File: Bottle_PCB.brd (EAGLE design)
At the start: 100 x 50 mm, 105 parts, among them Q1 8.000 MHz, Q2 ZVN 3306 F, Q3 ZVN 3306 F, Q4 ZVN 3306 F, Q5 ZVN 3306 F, Q6 ZVN 3306 F, Q7 ZVN 3306 F, U1 USD-SOCKETNEW

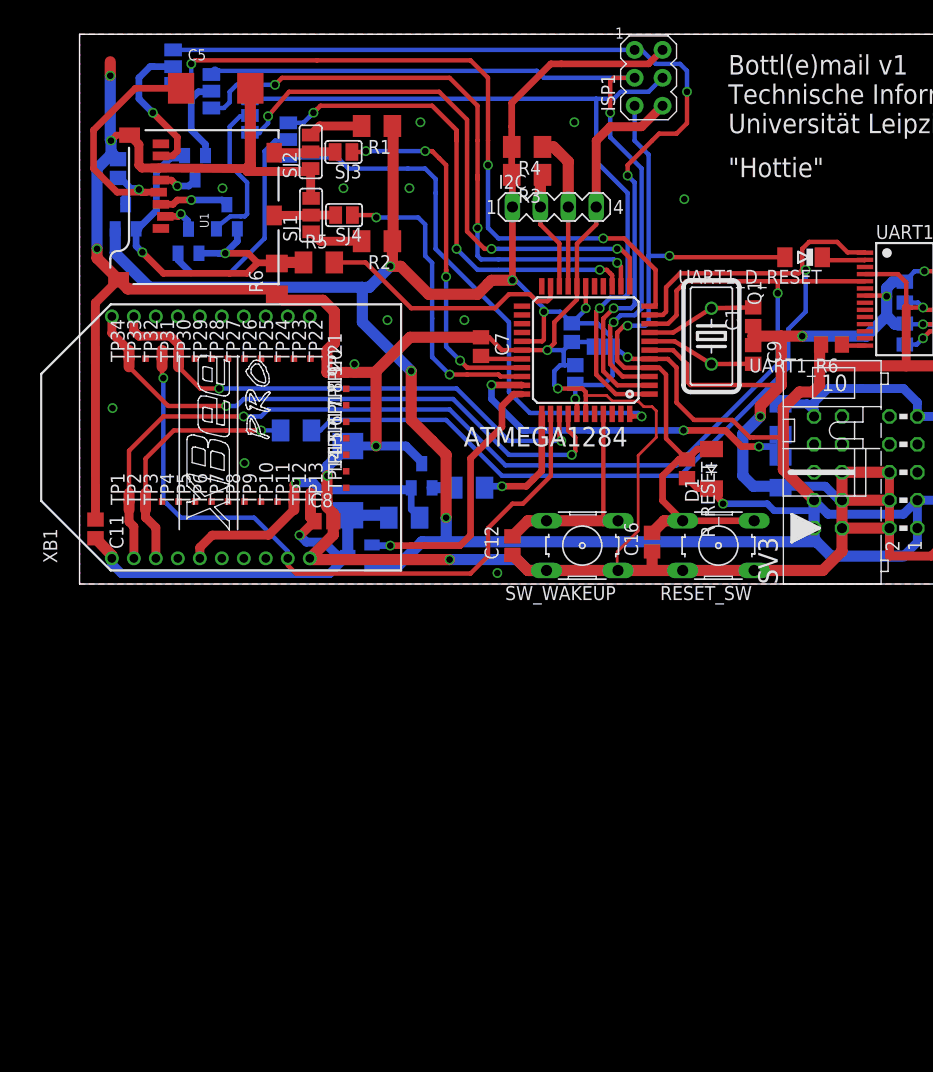
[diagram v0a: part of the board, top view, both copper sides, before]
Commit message: - Added Arduino Shield headers - cleaned up the schmeatic and grouped modules on sheets by function - inserted and de-crossed bus systems - started to unify font sizes and pin / netwrok naming
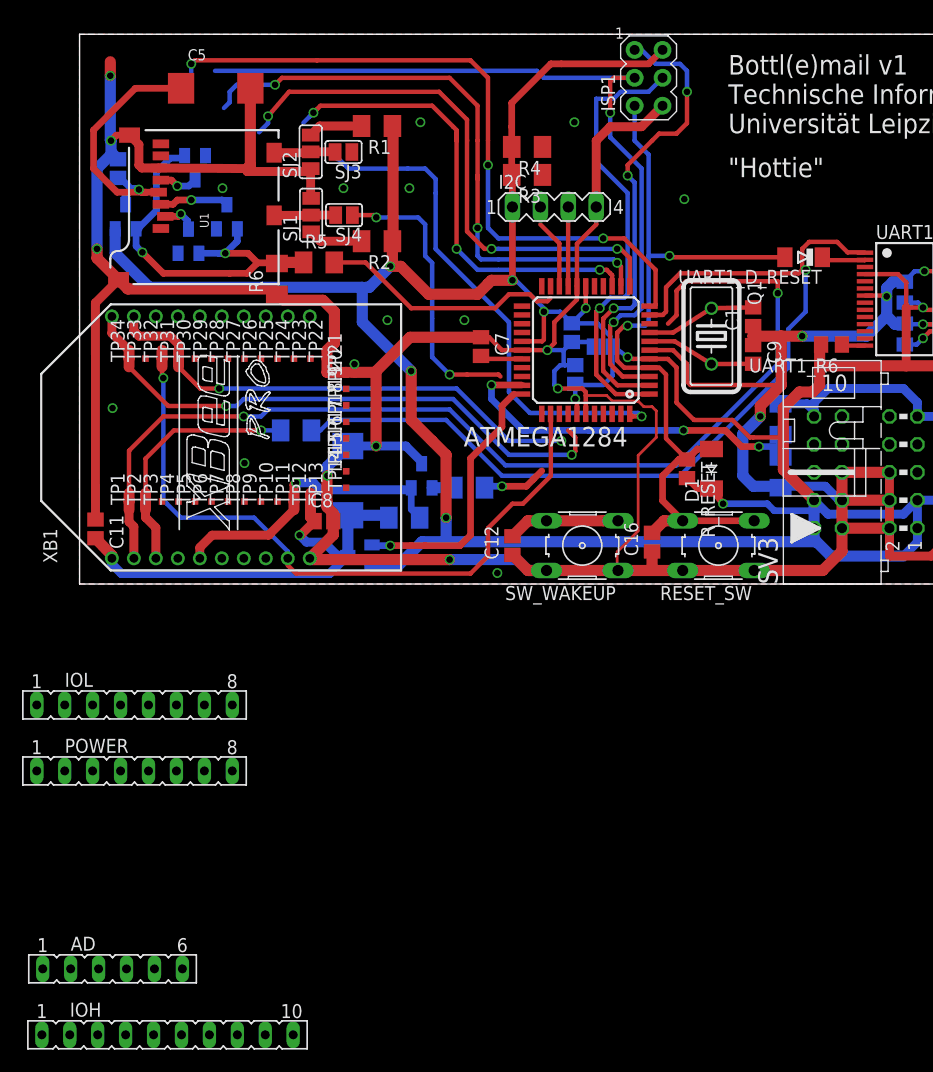
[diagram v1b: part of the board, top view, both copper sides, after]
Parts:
- removed SJ5, SJ6, SJ7, SJ8: (no value), jumper:SJ_2
- added AD: (no value), con-lsta:FE06
- added IOH: (no value), con-lsta:FE10
- added IOL, POWER: (no value), con-lsta:FE08
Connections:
- net VBATT_AIN0 renamed PB2_VBATT_AIN0
- net VBATT_AIN1 renamed PB3_VBATT_AIN1
- removed net INT_BUTTON: ATMEGA1284.41, C12.2, SW_WAKEUP.3, SW_WAKEUP.4
- removed net N$20: ATMEGA1284.31, SJ4.1
- removed net N$24: SJ5.2, U1.7
- removed net N$25: ATMEGA1284.30, SJ3.1
- removed net N$26: Q2.2, SJ6.2
- removed net N$27: Q3.2, SJ7.2
- removed net N$5: C_U12V.+, LM2594_3.3.7, R10.1, SV2.9, SV3.9, T_U12V.3
- removed net PB4/SS: ATMEGA1284.44, SJ8.1
- removed net PB5/MOSI: ATMEGA1284.1, ISP1.4, SJ7.1
- removed net PB6/MISO: ATMEGA1284.2, ISP1.1, SJ5.1
- removed net PB7/SCK: ATMEGA1284.3, ISP1.3, SJ6.1
- removed net PC0/I2C_SDL: ATMEGA1284.19, I2C.3, R4.1
- removed net PC1/I2C_SDA: ATMEGA1284.20, I2C.2, R3.1
- removed net PD5/CS: ATMEGA1284.14, SJ8.3
- removed net RXD1/MISO: ATMEGA1284.11, SJ5.3
- removed net SD_CS: Q4.2, SJ8.2
- removed net TXD1/MOSI: ATMEGA1284.12, SJ7.3
- removed net USB_BT_RXD0: ATMEGA1284.9, TP1.TP, UART1_IC2.5, XB1.2
- removed net USB_BT_TXD0: ATMEGA1284.10, R9.2, UART1_IC2.1
- removed net XCK1/SCK: ATMEGA1284.13, SJ6.3
- new net +5V: POWER.2, POWER.5
- new net N$7: SJ3.1
- new net PA0: AD.1, ATMEGA1284.37
- new net PA1: AD.2, ATMEGA1284.36
- new net PA2: AD.3, ATMEGA1284.35
- new net PA3: AD.4, ATMEGA1284.34
- new net PA4: AD.5, ATMEGA1284.33
- new net PA5: AD.6, ATMEGA1284.32
- new net PA6: SJ4.1
- new net PB0: ATMEGA1284.40, IOH.1
- new net PB1_INT_BUTTON: ATMEGA1284.41, C12.2, IOH.2, SW_WAKEUP.3, SW_WAKEUP.4
- new net PB4_SS: ATMEGA1284.44, IOH.3
- new net PB5_MOSI: ATMEGA1284.1, IOH.4, ISP1.4
- new net PB6_MISO: ATMEGA1284.2, IOH.5, ISP1.1
- new net PB7_SCK: ATMEGA1284.3, IOH.6, ISP1.3
- new net PC0_I2C_SDL: ATMEGA1284.19, I2C.3, IOH.10, R4.1
- new net PC1_I2C_SDA: ATMEGA1284.20, I2C.2, IOH.9, R3.1
- new net PD0_RXD0_USB: ATMEGA1284.9, UART1_IC2.5
- new net PD0_RXD0_USB_BT: IOL.1, TP1.TP, XB1.2
- new net PD1_TXD0_USB: ATMEGA1284.10, IOL.2, R9.2, UART1_IC2.1
- new net PD2_RXD1/MISO: ATMEGA1284.11, IOL.3, U1.7
- new net PD3_TXD1/MOSI: ATMEGA1284.12, IOL.4, Q3.2
- new net PD4_XCK1/SCK: ATMEGA1284.13, IOL.5, Q2.2
- new net PD5_CS: ATMEGA1284.14, IOL.6, Q4.2
- new net PD6: ATMEGA1284.15, IOL.7
- new net PD7: ATMEGA1284.16, IOL.8
- new net VIN: C_U12V.+, LM2594_3.3.7, POWER.8, R10.1, SV2.9, SV3.9, T_U12V.3
- net +3V3: now also POWER.4
- net AREF: now also IOH.8
- net BT_MODE: no longer ATMEGA1284.37
- net BT_PAIR: no longer ATMEGA1284.35
- net BT_RESET: no longer ATMEGA1284.34
- net BT_STATUS: no longer ATMEGA1284.36
- net BT_VCC_SIGNAL: no longer ATMEGA1284.33
- net GND: now also IOH.7, POWER.6, POWER.7
- net RESET: now also POWER.3
- net VBATT: no longer ATMEGA1284.32
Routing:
- net USB_BT_RXD0: track 106.5 -> 0.00 mm, vias 2 -> 0
- net PD0_RXD0_USB_BT: track 0.00 -> 96.9 mm, vias 0 -> 2
- net PB6/MISO: track 85.1 -> 0.00 mm, vias 3 -> 0
- net USB_BT_TXD0: track 85.0 -> 0.00 mm, vias 1 -> 0
- net PD1_TXD0_USB: track 0.00 -> 84.9 mm, vias 0 -> 1
- net PB7/SCK: track 74.1 -> 0.00 mm, vias 2 -> 0
- net PB7_SCK: track 0.00 -> 73.7 mm, vias 0 -> 2
- net PB5/MOSI: track 72.1 -> 0.00 mm, vias 1 -> 0
- net RXD1/MISO: track 65.2 -> 0.00 mm, vias 3 -> 0
- net PD2_RXD1/MISO: track 0.00 -> 64.0 mm, vias 0 -> 3
- net VIN: track 0.00 -> 63.6 mm, vias 0 -> 2
- net N$5: track 63.6 -> 0.00 mm, vias 2 -> 0
- net XCK1/SCK: track 56.2 -> 0.00 mm, vias 3 -> 0
- net PD4_XCK1/SCK: track 0.00 -> 55.0 mm, vias 0 -> 3
- net TXD1/MOSI: track 51.3 -> 0.00 mm, vias 3 -> 0
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
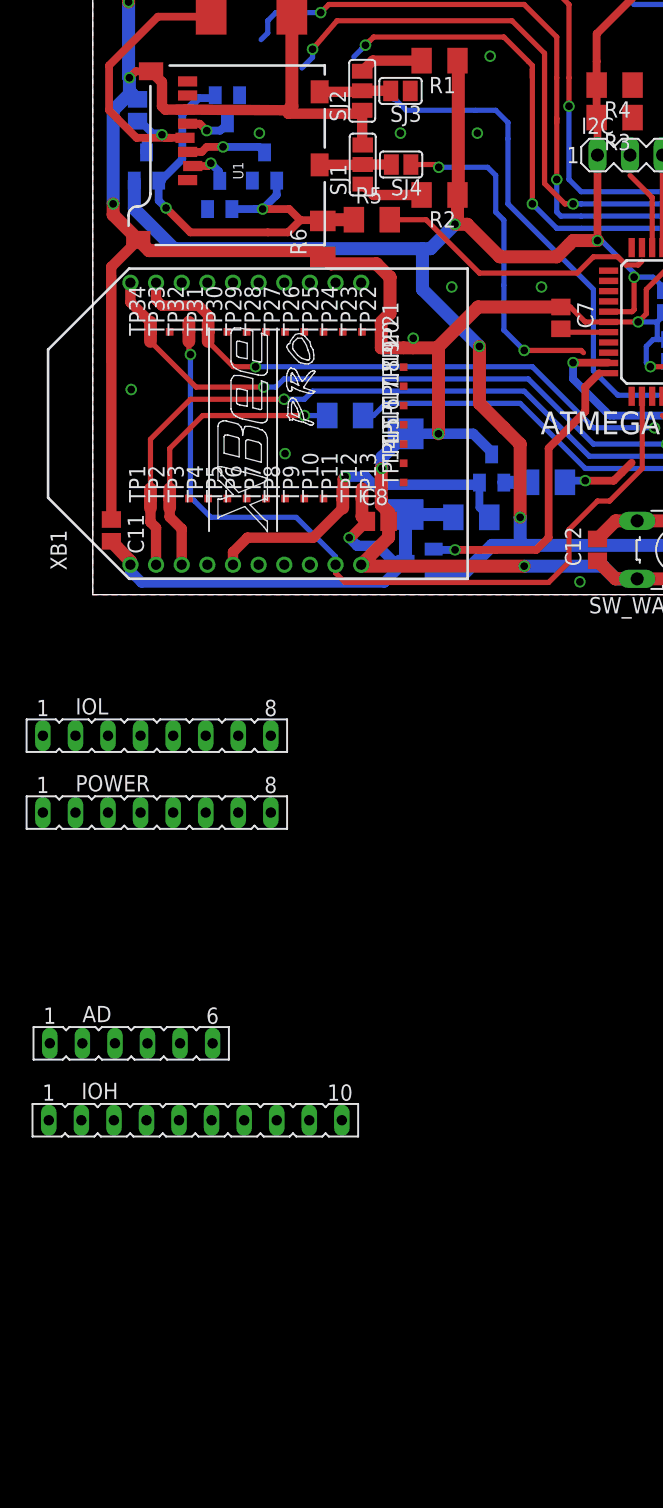
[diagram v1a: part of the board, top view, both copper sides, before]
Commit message: - employes Seeduino Open Parts Library for groove connectors and possibly more in the future - added groove connectors
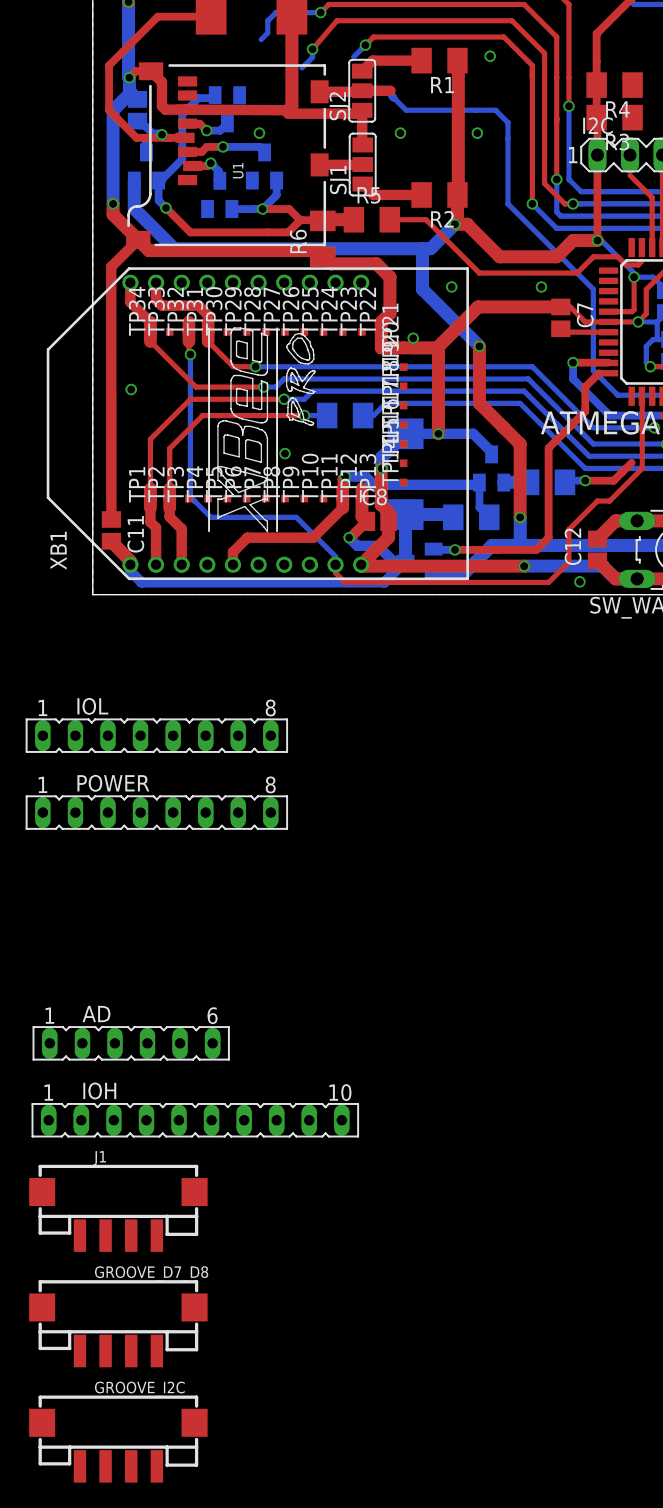
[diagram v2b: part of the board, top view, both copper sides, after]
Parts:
- removed SJ3, SJ4: (no value), jumper:SJ
- added GROOVE_D7_D8, GROOVE_I2C, J1: GROVE-4P-2.0-SMD, OPL:4P-SMD-2.0
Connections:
- removed net N$7: SJ3.1
- new net PA7: ATMEGA1284.30, J1.3
- net +3V3: now also GROOVE_D7_D8.2, GROOVE_I2C.2, J1.2
- net GND: now also GROOVE_D7_D8.1, GROOVE_I2C.1, J1.1
- net N$16: no longer SJ3.2
- net N$17: no longer SJ4.2
- net PA6: now also ATMEGA1284.31, J1.4; no longer SJ4.1
- net PB0: now also GROOVE_D7_D8.3
- net PC0_I2C_SDL: now also GROOVE_I2C.3
- net PC1_I2C_SDA: now also GROOVE_I2C.4
- net PD7: now also GROOVE_D7_D8.4
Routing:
- net PA6: track 26.2 -> 0.00 mm, vias 2 -> 0
- net N$17: track 5.61 -> 3.37 mm
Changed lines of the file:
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@@
 <layer number="97" name="Info" color="7" fill="1" visible="no" active="no"/>
 <layer number="98" name="Guide" color="6" fill="1" visible="no" active="no"/>
+<layer number="99" name="SpiceOrder" color="5" fill="1" visible="no" active="no"/>
 <layer number="100" name="Mechanical" color="7" fill="1" visible="no" active="yes"/>
 <layer number="101" name="Gehäuse" color="7" fill="1" visible="no" active="yes"/>
@@
 <layer number="111" name="LPC17xx" color="7" fill="1" visible="yes" active="yes"/>
 <layer number="112" name="tSilk" color="7" fill="1" visible="yes" active="yes"/>
+<layer number="113" name="IDFDebug" color="7" fill="1" visible="no" active="yes"/>
 <layer number="116" name="Patch_BOT" color="9" fill="4" visible="yes" active="yes"/>
+<layer number="118" name="Rect_Pads" color="7" fill="1" visible="no" active="no"/>
 <layer number="121" name="_tsilk" color="7" fill="1" visible="yes" active="yes"/>
 <layer number="122" name="_bsilk" color="7" fill="1" visible="yes" active="yes"/>
@@
 <layer number="223" name="223bmp" color="24" fill="1" visible="no" active="no"/>
 <layer number="224" name="224bmp" color="25" fill="1" visible="no" active="no"/>
+<layer number="225" name="225bmp" color="7" fill="1" visible="no" active="yes"/>
+<layer number="226" name="226bmp" color="7" fill="1" visible="no" active="yes"/>
+<layer number="227" name="227bmp" color="7" fill="1" visible="no" active="yes"/>
+<layer number="228" name="228bmp" color="7" fill="1" visible="no" active="yes"/>
+<layer number="230" name="230bmp" color="7" fill="1" visible="no" active="yes"/>
 <layer number="248" name="Housing" color="7" fill="1" visible="yes" active="yes"/>
 <layer number="249" name="Edge" color="7" fill="1" visible="yes" active="yes"/>
@@
 <element name="SJ1" library="jumper" package="SJ_2" value="" x="21.0566" y="33.5534" rot="R90"/>
 <element name="SJ2" library="jumper" package="SJ_2" value="" x="21.0185" y="39.3065" rot="R90"/>
-<element name="SJ3" library="jumper" package="SJ" value="" x="24.003" y="39.2938" rot="R180"/>
-<element name="SJ4" library="jumper" package="SJ" value="" x="24.0538" y="33.5534" rot="R180"/>
 <element name="R1" library="rcl" package="M1206" value="50k" x="27.051" y="41.656" rot="R180"/>
 <element name="R2" library="rcl" package="M1206" value="50k" x="27.051" y="31.1785" rot="R180"/>
@@
 <attribute name="OC_FARNELL" value="unknown" x="8" y="-41" size="1.778" layer="27" display="off"/>
 </element>
+<element name="J1" library="OPL" package="4P-SMD-2.0" value="GROVE-4P-2.0-SMD" x="2" y="-50"/>
+<element name="GROOVE_D7_D8" library="OPL" package="4P-SMD-2.0" value="GROVE-4P-2.0-SMD" x="2" y="-59"/>
+<element name="GROOVE_I2C" library="OPL" package="4P-SMD-2.0" value="GROVE-4P-2.0-SMD" x="2" y="-68"/>
 </elements>
 <signals>
@@
 <contactref element="POWER" pad="7"/>
 <contactref element="POWER" pad="6"/>
+<contactref element="GROOVE_I2C" pad="1"/>
+<contactref element="GROOVE_D7_D8" pad="1"/>
+<contactref element="J1" pad="1"/>
 <wire x1="51.1175" y1="41.5925" x2="55" y2="35" width="0" layer="19" extent="1-1"/>
 <wire x1="25" y1="20" x2="25" y2="19.25" width="0" layer="19" extent="1-1"/>
@@
 <wire x1="8.81" y1="-17" x2="11.35" y2="-17" width="0" layer="19" extent="1-1"/>
 <wire x1="11.81" y1="-41" x2="11.35" y2="-17" width="0" layer="19" extent="1-1"/>
+<wire x1="-1" y1="-50" x2="11.81" y2="-41" width="0" layer="19" extent="1-1"/>
+<wire x1="-1" y1="-59" x2="-1" y2="-50" width="0" layer="19" extent="1-1"/>
+<wire x1="-1" y1="-68" x2="-1" y2="-59" width="0" layer="19" extent="1-1"/>
 </signal>
 <signal name="AREF">
@@
 <contactref element="R3" pad="1"/>
 <contactref element="I2C" pad="2"/>
+<contactref element="GROOVE_I2C" pad="4"/>
 <wire x1="41.91" y1="34.29" x2="42.1035" y2="37.211" width="0" layer="19" extent="1-1"/>
 <wire x1="41.91" y1="32.7025" x2="41.91" y2="34.29" width="0" layer="19" extent="1-1"/>
 <wire x1="16.89" y1="-41" x2="43.6375" y2="27.0725" width="0" layer="19" extent="1-1"/>
+<wire x1="5" y1="-68" x2="16.89" y2="-41" width="0" layer="19" extent="1-1"/>
 </signal>
 <signal name="PC0_I2C_SDL">
@@
 <contactref element="I2C" pad="3"/>
 <contactref element="R4" pad="1"/>
+<contactref element="GROOVE_I2C" pad="3"/>
 <wire x1="44.45" y1="34.29" x2="42.1035" y2="39.751" width="0" layer="19" extent="1-1"/>
 <wire x1="44.4375" y1="34.2775" x2="44.45" y2="34.29" width="0" layer="19" extent="1-1"/>
 <wire x1="19.43" y1="-41" x2="44.4375" y2="27.0725" width="0" layer="19" extent="1-1"/>
+<wire x1="3" y1="-68" x2="19.43" y2="-41" width="0" layer="19" extent="1-1"/>
 </signal>
 <signal name="N$3">
@@
 <wire x1="51.7525" y1="47.3075" x2="53.0225" y2="48.5775" width="0.6096" layer="1"/>
 <contactref element="POWER" pad="4"/>
-<wire x1="3.73" y1="-17" x2="26.595" y2="1.6535" width="0" layer="19" extent="16-16"/>
+<contactref element="GROOVE_I2C" pad="2"/>
+<contactref element="GROOVE_D7_D8" pad="2"/>
+<contactref element="J1" pad="2"/>
+<wire x1="1" y1="-59" x2="1" y2="-68" width="0" layer="19" extent="1-1"/>
+<wire x1="1" y1="-50" x2="1" y2="-59" width="0" layer="19" extent="1-1"/>
+<wire x1="3.73" y1="-17" x2="1" y2="-50" width="0" layer="19" extent="1-1"/>
+<wire x1="26.595" y1="1.6535" x2="3.73" y2="-17" width="0" layer="19" extent="16-16"/>
 </signal>
 <signal name="N$16">
 <contactref element="SJ2" pad="2"/>
-<contactref element="SJ3" pad="2"/>
 <contactref element="U1" pad="CD1"/>
 <wire x1="17.6975" y1="39.225" x2="20.937" y2="39.225" width="0.8128" layer="1"/>
 <wire x1="20.937" y1="39.225" x2="21.0185" y2="39.3065" width="0.8128" layer="1"/>
 <wire x1="21.0185" y1="39.3065" x2="23.2283" y2="39.3065" width="0.8128" layer="1"/>
-<wire x1="23.2283" y1="39.3065" x2="23.241" y2="39.2938" width="0.8128" layer="1"/>
 </signal>
 <signal name="N$17">
 <contactref element="SJ1" pad="2"/>
-<contactref element="SJ4" pad="2"/>
 <contactref element="U1" pad="CD2"/>
 <wire x1="17.6975" y1="33.525" x2="21.0282" y2="33.525" width="0.8128" layer="1"/>
 <wire x1="21.0282" y1="33.525" x2="21.0566" y2="33.5534" width="0.8128" layer="1"/>
-<wire x1="21.0566" y1="33.5534" x2="23.2918" y2="33.5534" width="0.8128" layer="1"/>
 </signal>
 <signal name="N$21">
@@
 <wire x1="71.4025" y1="30.1625" x2="71.432" y2="30.133" width="0" layer="19" extent="1-1"/>
 <wire x1="-1.35" y1="-11" x2="21.085" y2="13.97" width="0" layer="19" extent="16-16"/>
-</signal>
-<signal name="PA6">
-<contactref element="SJ4" pad="1"/>
-<wire x1="38.2775" y1="18.8725" x2="38.1" y2="19.05" width="0.4064" layer="1"/>
-<wire x1="38.1" y1="19.05" x2="35.2425" y2="19.05" width="0.4064" layer="1"/>
-<wire x1="35.2425" y1="19.05" x2="33.655" y2="19.05" width="0.4064" layer="1"/>
-<via x="33.655" y="19.05" extent="1-16" drill="0.6"/>
-<wire x1="33.655" y1="19.05" x2="32.0675" y2="20.6375" width="0.4064" layer="16"/>
-<wire x1="32.0675" y1="20.6375" x2="32.0675" y2="24.13" width="0.4064" layer="16"/>
-<wire x1="32.0675" y1="24.13" x2="32.0675" y2="29.21" width="0.4064" layer="16"/>
-<wire x1="32.0675" y1="29.21" x2="31.4325" y2="29.845" width="0.4064" layer="16"/>
-<wire x1="24.8158" y1="33.5534" x2="26.7716" y2="33.5534" width="0.4064" layer="1"/>
-<wire x1="26.7716" y1="33.5534" x2="26.9875" y2="33.3375" width="0.4064" layer="1"/>
-<via x="26.9875" y="33.3375" extent="1-16" drill="0.6"/>
-<wire x1="26.9875" y1="33.3375" x2="30.7975" y2="33.3375" width="0.4064" layer="16"/>
-<wire x1="30.7975" y1="33.3375" x2="31.4325" y2="32.7025" width="0.4064" layer="16"/>
-<wire x1="31.4325" y1="32.7025" x2="31.4325" y2="29.845" width="0.4064" layer="16"/>
 </signal>
 <signal name="PB4_SS">
@@
 <contactref element="ATMEGA1284" pad="16"/>
 <contactref element="IOL" pad="8"/>
+<contactref element="GROOVE_D7_D8" pad="4"/>
 <wire x1="13.89" y1="-11" x2="46.8375" y2="27.0725" width="0" layer="19" extent="1-1"/>
+<wire x1="5" y1="-59" x2="13.89" y2="-11" width="0" layer="19" extent="1-1"/>
 </signal>
 <signal name="PB0">
 <contactref element="ATMEGA1284" pad="40"/>
 <contactref element="IOH" pad="1"/>
+<contactref element="GROOVE_D7_D8" pad="3"/>
 <wire x1="-3.43" y1="-41" x2="46.8375" y2="15.4725" width="0" layer="19" extent="1-1"/>
+<wire x1="3" y1="-59" x2="-3.43" y2="-41" width="0" layer="19" extent="1-1"/>
 </signal>
 <signal name="PA0">
@@
 <wire x1="9.35" y1="-35" x2="40.2375" y2="18.0725" width="0" layer="19" extent="1-1"/>
 </signal>
-<signal name="N$7">
-<contactref element="SJ3" pad="1"/>
-</signal>
 <signal name="+5V">
 <contactref element="POWER" pad="5"/>
@@
 <wire x1="6.27" y1="-17" x2="-1.35" y2="-17" width="0" layer="19" extent="1-1"/>
 </signal>
+<signal name="PA6">
+<contactref element="ATMEGA1284" pad="31"/>
+<contactref element="J1" pad="4"/>
+<wire x1="5" y1="-50" x2="40.2375" y2="18.8725" width="0" layer="19" extent="1-1"/>
+</signal>
+<signal name="PA7">
+<contactref element="ATMEGA1284" pad="30"/>
+<contactref element="J1" pad="3"/>
+<wire x1="3" y1="-50" x2="40.2375" y2="19.6725" width="0" layer="19" extent="1-1"/>
+</signal>
 </signals>
